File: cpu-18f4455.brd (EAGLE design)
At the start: 67.3 x 20 mm, 9 parts, among them IC1 PIC18F4455

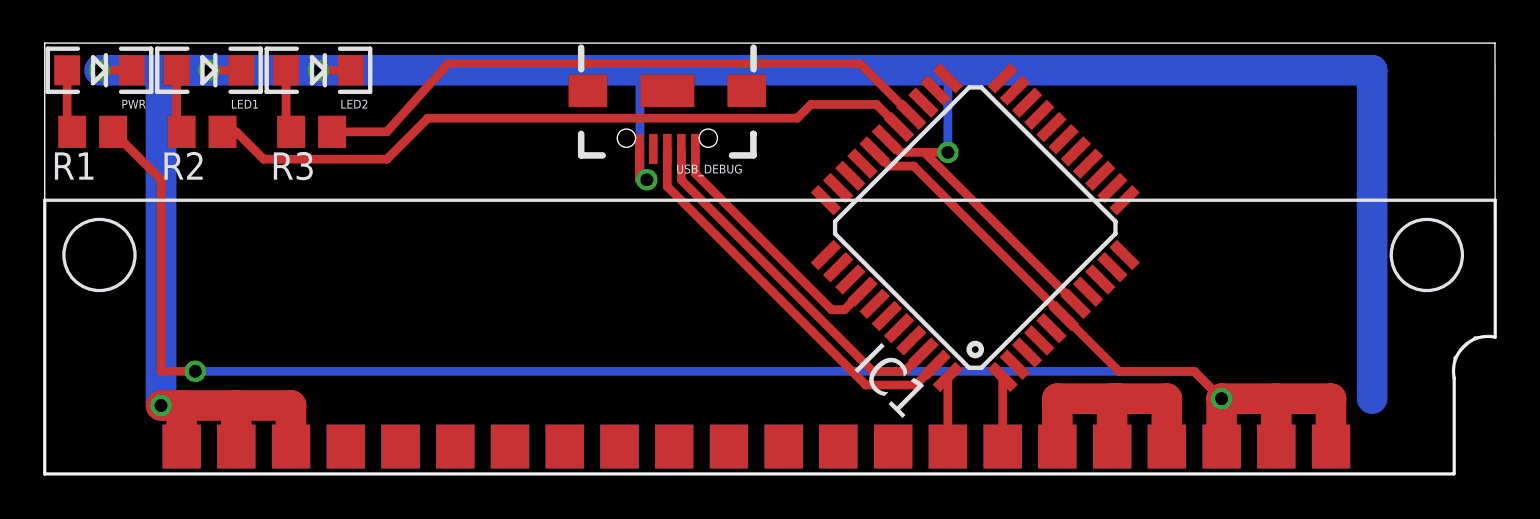
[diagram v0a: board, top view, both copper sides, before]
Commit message: I wired power backwards. I am the dumb. ._.;
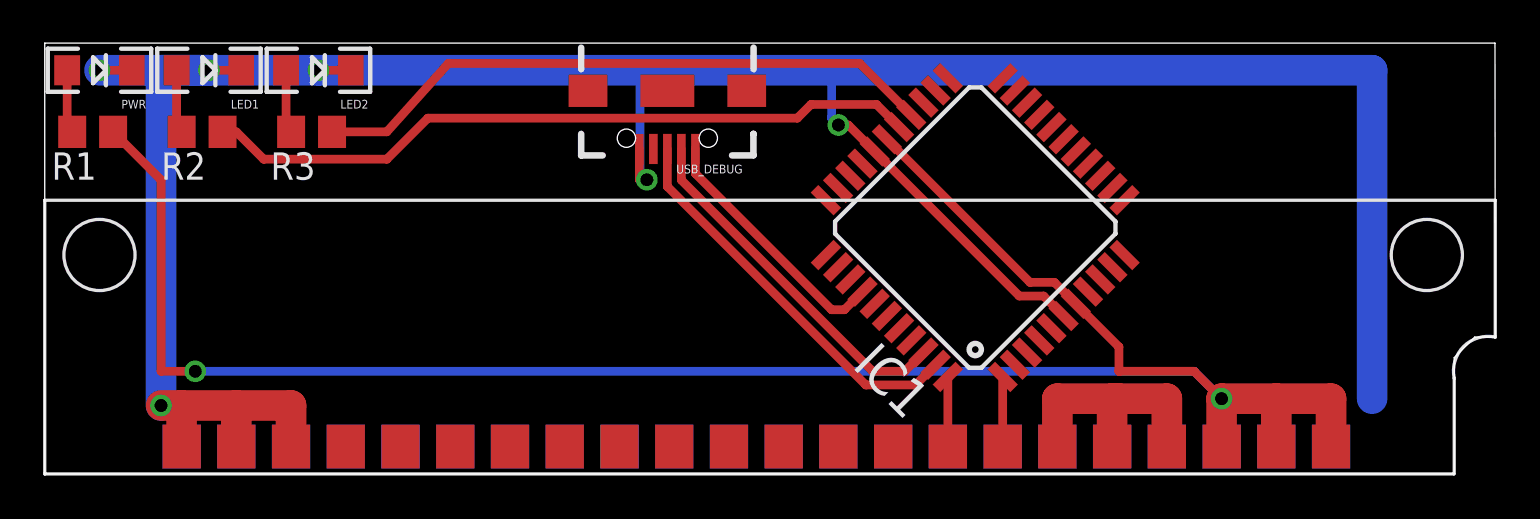
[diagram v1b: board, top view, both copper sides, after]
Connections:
- removed net ?: IC1.8
- removed net N$8: IC1.9
- net +3V3: now also IC1.28, IC1.7; no longer IC1.29, IC1.6
- net GND: now also IC1.29, IC1.6; no longer IC1.28, IC1.7
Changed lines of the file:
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@@
 <signals>
 <signal name="GND">
-<contactref element="IC1" pad="7"/>
-<contactref element="IC1" pad="28"/>
 <contactref element="USB_DEBUG" pad="GND1"/>
 <contactref element="IO" pad="20T"/>
@@
 <wire x1="11.43" y1="1.27" x2="11.43" y2="3.175" width="1.4224" layer="1"/>
 <wire x1="11.43" y1="3.175" x2="8.89" y2="3.175" width="1.4224" layer="1"/>
-<wire x1="47.846903125" y1="7.894465625" x2="40.81886875" y2="14.9225" width="0.4064" layer="1"/>
 <wire x1="12.7" y1="18.7325" x2="27.6225" y2="18.7325" width="1.4224" layer="16"/>
-<wire x1="27.6225" y1="18.7325" x2="41.91" y2="18.7325" width="1.4224" layer="16"/>
-<wire x1="41.91" y1="18.7325" x2="61.595" y2="18.7325" width="1.4224" layer="16"/>
+<wire x1="27.6225" y1="18.7325" x2="36.5125" y2="18.7325" width="1.4224" layer="16"/>
+<wire x1="36.5125" y1="18.7325" x2="61.595" y2="18.7325" width="1.4224" layer="16"/>
 <wire x1="61.595" y1="18.7325" x2="61.595" y2="3.4925" width="1.4224" layer="16"/>
-<wire x1="39.078778125" y1="15.53121875" x2="39.687496875" y2="14.9225" width="0.4064" layer="1"/>
-<wire x1="39.687496875" y1="14.9225" x2="40.81886875" y2="14.9225" width="0.4064" layer="1"/>
-<wire x1="40.81886875" y1="14.9225" x2="41.91" y2="14.9225" width="0.4064" layer="1"/>
-<via x="41.91" y="14.9225" extent="1-16" drill="0.6" shape="square"/>
-<wire x1="41.91" y1="14.9225" x2="41.91" y2="18.7325" width="0.4064" layer="16"/>
 <wire x1="27.5925" y1="15.08" x2="27.5925" y2="13.6525" width="0.4064" layer="1"/>
 <wire x1="27.5925" y1="13.6525" x2="27.94" y2="13.6525" width="0.4064" layer="1"/>
@@
 <wire x1="27.94" y1="13.6525" x2="27.6225" y2="13.6525" width="0.4064" layer="16"/>
 <wire x1="27.6225" y1="13.6525" x2="27.6225" y2="18.7325" width="0.4064" layer="16"/>
+<contactref element="IC1" pad="29"/>
+<contactref element="IC1" pad="6"/>
+<wire x1="38.51309375" y1="14.96553125" x2="45.223625" y2="8.255" width="0.4064" layer="1"/>
+<wire x1="45.223625" y1="8.255" x2="46.354996875" y2="8.255" width="0.4064" layer="1"/>
+<wire x1="47.28121875" y1="7.328778125" x2="46.354996875" y2="8.255" width="0.4064" layer="1"/>
+<wire x1="38.51309375" y1="14.96553125" x2="37.286125" y2="16.1925" width="0.4064" layer="1"/>
+<wire x1="37.286125" y1="16.1925" x2="36.83" y2="16.1925" width="0.4064" layer="1"/>
+<via x="36.83" y="16.1925" extent="1-16" drill="0.6" shape="square"/>
+<wire x1="36.83" y1="16.1925" x2="36.5125" y2="16.51" width="0.4064" layer="16"/>
+<wire x1="36.5125" y1="16.51" x2="36.5125" y2="18.7325" width="0.4064" layer="16"/>
 </signal>
 <signal name="+3V3">
-<contactref element="IC1" pad="6"/>
-<contactref element="IC1" pad="29"/>
 <contactref element="IO" pad="1T"/>
 <contactref element="IO" pad="2T"/>
@@
 <wire x1="54.61" y1="1.27" x2="54.61" y2="3.4925" width="1.4224" layer="1"/>
 <wire x1="57.15" y1="1.27" x2="57.15" y2="3.4925" width="1.4224" layer="1"/>
-<wire x1="47.28121875" y1="7.328778125" x2="49.847496875" y2="4.7625" width="0.4064" layer="1"/>
-<wire x1="49.847496875" y1="4.7625" x2="53.34" y2="4.7625" width="0.4064" layer="1"/>
+<wire x1="49.847496875" y1="4.7625" x2="49.8475" y2="4.7625" width="0.4064" layer="1"/>
+<wire x1="49.8475" y1="4.7625" x2="53.34" y2="4.7625" width="0.4064" layer="1"/>
 <wire x1="53.34" y1="4.7625" x2="54.61" y2="3.4925" width="0.4064" layer="1"/>
-<wire x1="47.28121875" y1="7.328778125" x2="40.322496875" y2="14.2875" width="0.4064" layer="1"/>
-<wire x1="40.322496875" y1="14.2875" x2="39.191125" y2="14.2875" width="0.4064" layer="1"/>
-<wire x1="38.51309375" y1="14.96553125" x2="39.191125" y2="14.2875" width="0.4064" layer="1"/>
 <wire x1="3.1725" y1="15.875" x2="5.3975" y2="13.65" width="0.4064" layer="1"/>
 <wire x1="5.3975" y1="13.65" x2="5.3975" y2="4.7625" width="0.4064" layer="1"/>
@@
 <wire x1="53.34" y1="4.7625" x2="54.61" y2="3.4925" width="0.4064" layer="16"/>
 <via x="54.61" y="3.4925" extent="1-16" drill="0.6" shape="square"/>
+<contactref element="IC1" pad="28"/>
+<contactref element="IC1" pad="7"/>
+<wire x1="39.078778125" y1="15.53121875" x2="45.719996875" y2="8.89" width="0.4064" layer="1"/>
+<wire x1="45.719996875" y1="8.89" x2="46.85136875" y2="8.89" width="0.4064" layer="1"/>
+<wire x1="47.846903125" y1="7.894465625" x2="46.85136875" y2="8.89" width="0.4064" layer="1"/>
+<wire x1="47.846903125" y1="7.894465625" x2="49.8475" y2="5.89386875" width="0.4064" layer="1"/>
+<wire x1="49.8475" y1="5.89386875" x2="49.8475" y2="4.7625" width="0.4064" layer="1"/>
 </signal>
 <signal name="N$3">
@@
 <wire x1="40.21015" y1="16.6625875" x2="37.8227375" y2="19.05" width="0.4064" layer="1"/>
 </signal>
-<signal name="N$8">
-<contactref element="IC1" pad="9"/>
-</signal>
-<signal name="?">
-<contactref element="IC1" pad="8"/>
-</signal>
 <signal name="N$7">
